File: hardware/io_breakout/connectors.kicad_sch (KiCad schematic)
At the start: 9 parts, among them J1 IDC26, J2 12-way 5.08, J3 12-way 5.08

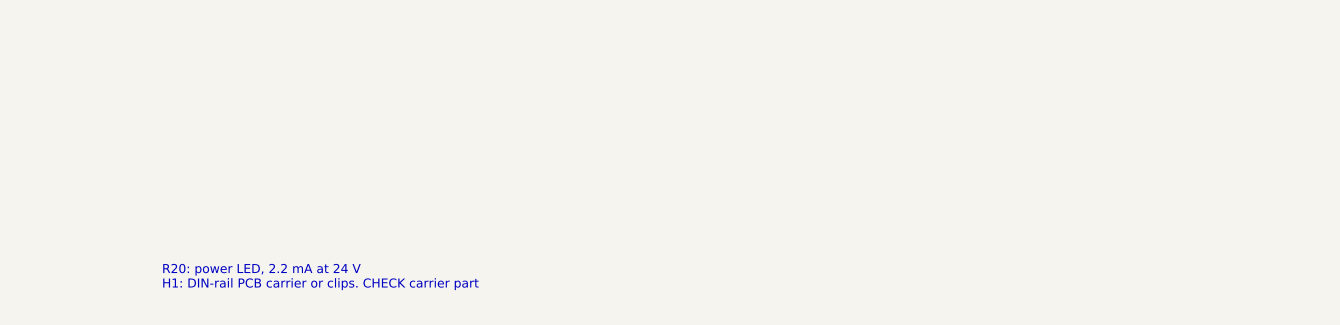
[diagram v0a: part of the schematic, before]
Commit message: CORE PCB: layout start in BC 215,6 outline; breakout header and carrier chosen
gen_pcb.py writes cems_core.kicad_pcb from design.py: 4 layers, assumed BC 215,6
outline (211.5 x 85.1 mm; BC 161,6 is too small for the I/O section), all 423
footprints with nets, connectors on the housing faces, a block plan per sheet, net
classes and 2.5 mm isolation rules between the four ground domains. Placeholder
PG-VQFN-70 footprint for the ISO2H823V2.5 (to redraw). Breakout: Wurth 61202622821
latched header, board 50 x 80 mm for a standard DIN PCB holder.

Co-Authored-By: Claude Opus 5.5 <noreply@anthropic.com>
Claude-Session: https://claude.ai/code/session_014onnq3eRiDkqdAB6fKiRDW
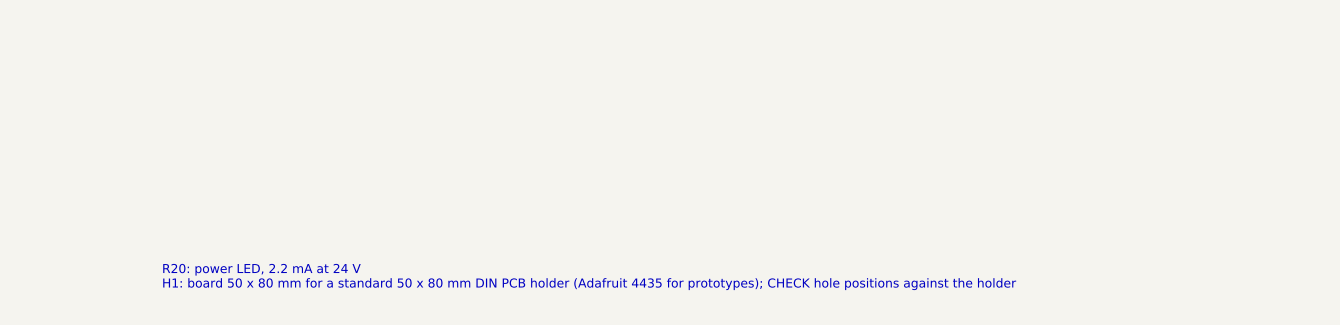
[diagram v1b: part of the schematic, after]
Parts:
- J1: MPN 26-way 2.54 mm shrouded box header with ejector latches (Wu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 -> Wurth 61202622821 (WR-BHD, 26-way, long latches, 3 A per co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
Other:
- note added: "R20: power LED, 2.2 mA at 24 V H1: board 50 x 80 mm for a standard 50 x 80 mm DIN PCB holder (Adafruit 4435 for prototypes); CHECK hole positions against the holder"
- note removed: "R20: power LED, 2.2 mA at 24 V H1: DIN-rail PCB carrier or clips. CHECK carrier part"
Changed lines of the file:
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@@
     (effects (font (size 1.0 1.0)) (justify left top))
   )
-  (text "\nR20: power LED, 2.2 mA at 24 V\nH1: DIN-rail PCB carrier or clips. CHECK carrier part"
+  (text "\nR20: power LED, 2.2 mA at 24 V\nH1: board 50 x 80 mm for a standard 50 x 80 mm DIN PCB holder (Adafruit 4435 for prototypes); CHECK hole positions against the holder"
     (at 147.32 137.16 0)
     (effects (font (size 1.0 1.0)) (justify left top))
@@
       (effects (font (size 1.27 1.27)) hide)
     )
-    (property "MPN" "26-way 2.54 mm shrouded box header with ejector latches (Wurth, Amphenol or TE), 1 A per contact. CHECK MPN" (id 4) (at 33.02 35.56 0)
+    (property "MPN" "Wurth 61202622821 (WR-BHD, 26-way, long latches, 3 A per contact; RS 771-8446)" (id 4) (at 33.02 35.56 0)
       (effects (font (size 1.27 1.27)) hide)
     )

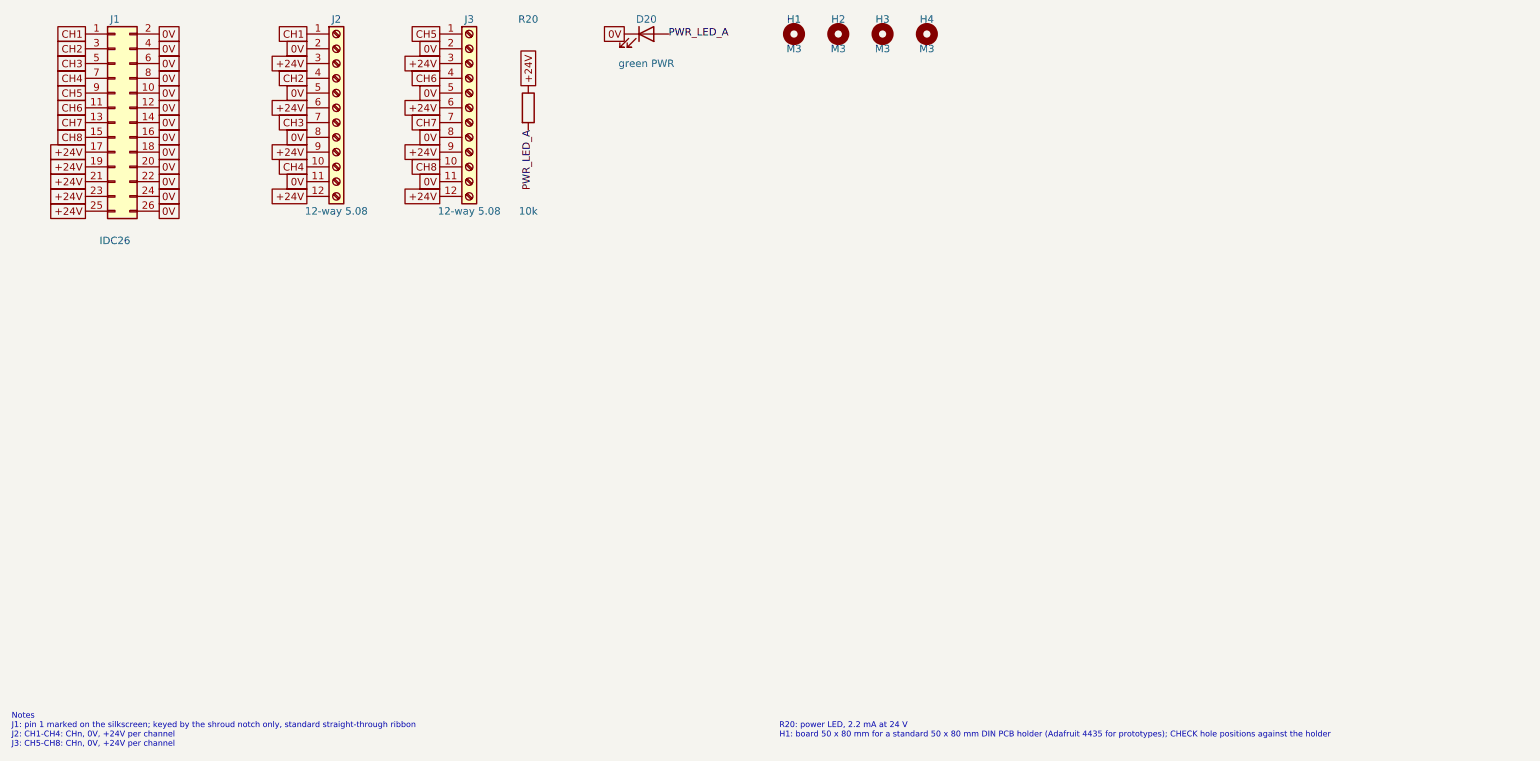
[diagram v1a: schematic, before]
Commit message: One 40-way ribbon for all digital I/O (Gary, 31 Oct)
Main board: J10 becomes a 40-way latched IDC header carrying bank A outputs 1-8 (pins
1-16, each beside its 0 V) and inputs 1-8 (pins 17-32), with 4 x +24 V and 4 x 0 V; J12
and F11 removed, so no ribbon can go into the wrong slot. Breakout rev 0.2: one board,
50 x 80 mm, two-tier 3.81 mm pluggable headers (valves OUT over 0V, inputs IN over +24V,
plus a 0V strip for 3-wire sensors), LEDs on every channel, flyback options on the valves.
Two-tier footprint is a placeholder until the maker's drawing is checked.

Co-Authored-By: Claude Opus 5.5 <noreply@anthropic.com>
Claude-Session: https://claude.ai/code/session_014onnq3eRiDkqdAB6fKiRDW
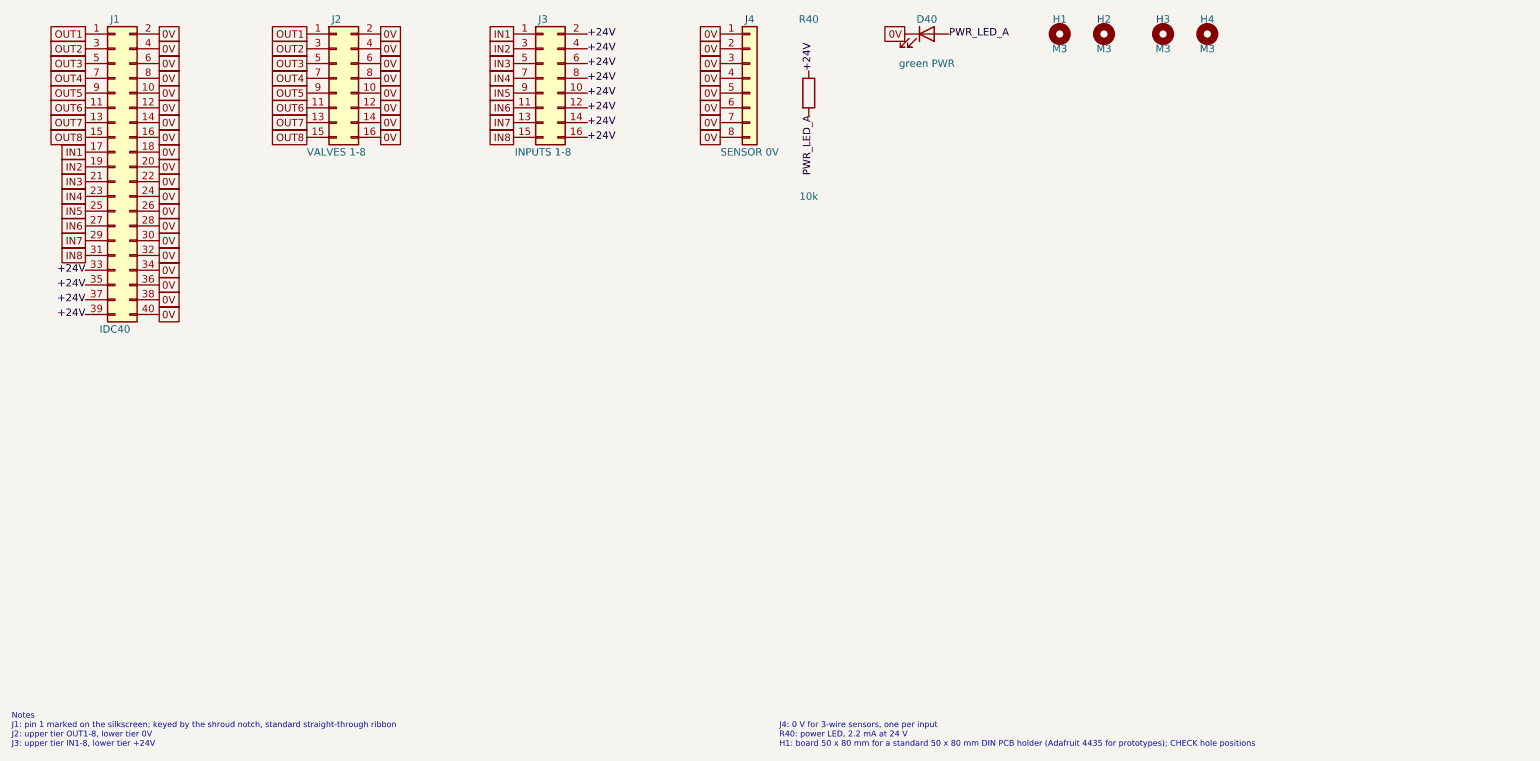
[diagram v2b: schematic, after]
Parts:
- removed D20: green PWR, LED_SMD:LED_0805_2012Metric, symbol Device:LED
- removed R20: 10k, Resistor_SMD:R_0805_2012Metric, symbol Device:R
- added D40: green PWR, LED_SMD:LED_0805_2012Metric, symbol Device:LED
- added J4: SENSOR 0V, Connector_Phoenix_MC:PhoenixContact_MCV_1,5_8-G-3.81_1x08_P3.81mm_Vertical, symbol Connector_Generic:Conn_01x08
- added R40: 10k, Resistor_SMD:R_0805_2012Metric, symbol Device:R
- J1: value IDC26 -> IDC40; footprint Connector_IDC:IDC-Header_2x13_P2.54mm_Latch_Vertical -> Connector_IDC:IDC-Header_2x20_P2.54mm_Latch_Vertical; symbol Connector_Generic:Conn_02x13_Odd_Even -> Connector_Generic:Conn_02x20_Odd_Even; MPN Wurth 61202622821 (WR-BHD, 26-way, long latches, 3 A per co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 -> Wurth 61204022821 (WR-BHD 40-way, long latches, 3 A per con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
- J2: value 12-way 5.08 -> VALVES 1-8; footprint TerminalBlock_Phoenix:TerminalBlock_Phoenix_MKDS-1,5-12-5.08_1x12_P5.08mm_Horizontal -> cems_io_breakout:Phoenix_MCDV_1,5_8-G-3.81_2x08_P3.81mm_TwoLevel; symbol Connector:Screw_Terminal_01x12 -> Connector_Generic:Conn_02x08_Odd_Even; MPN Degson or Dinkle 5.08 mm PCB screw terminal, 12-way, UL, 30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 -> Phoenix MCDV 1,5/8-G-3,81 two-level header + 2 x MCVR plugs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
- J3: value 12-way 5.08 -> INPUTS 1-8; footprint TerminalBlock_Phoenix:TerminalBlock_Phoenix_MKDS-1,5-12-5.08_1x12_P5.08mm_Horizontal -> cems_io_breakout:Phoenix_MCDV_1,5_8-G-3.81_2x08_P3.81mm_TwoLevel; symbol Connector:Screw_Terminal_01x12 -> Connector_Generic:Conn_02x08_Odd_Even; MPN Degson or Dinkle 5.08 mm PCB screw terminal, 12-way, UL, 30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 -> as J2
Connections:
- net +24V: now also J1.33 (Pin_33), J1.35 (Pin_35), J1.37 (Pin_37), J1.39 (Pin_39), J3.10 (Pin_10), J3.14 (Pin_14), J3.16 (Pin_16), J3.2 (Pin_2), J3.4 (Pin_4), J3.8 (Pin_8), R40.1; no longer J1.17 (Pin_17), J1.19 (Pin_19), J1.21 (Pin_21), J1.23 (Pin_23), J1.25 (Pin_25), J2.12 (Pin_12), J2.3 (Pin_3), J2.6 (Pin_6), J2.9 (Pin_9), J3.3 (Pin_3), J3.9 (Pin_9)
- net 0V: now also J1.28 (Pin_28), J1.30 (Pin_30), J1.32 (Pin_32), J1.34 (Pin_34), J1.36 (Pin_36), J1.38 (Pin_38), J1.40 (Pin_40), J2.10 (Pin_10), J2.12 (Pin_12), J2.14 (Pin_14), J2.16 (Pin_16), J2.4 (Pin_4), J2.6 (Pin_6), D40.1 (K), J4.1 (Pin_1), J4.2 (Pin_2), J4.3 (Pin_3), J4.4 (Pin_4), J4.5 (Pin_5), J4.6 (Pin_6), J4.7 (Pin_7), J4.8 (Pin_8); no longer J2.11 (Pin_11), J2.5 (Pin_5), J3.11 (Pin_11), J3.2 (Pin_2), J3.5 (Pin_5), J3.8 (Pin_8)
- net PWR_LED_A: now also D40.2 (A), R40.2
- net CH1 renamed OUT1
- net CH2 renamed OUT2
- net OUT2: now also J2.3 (Pin_3); no longer J2.4 (Pin_4)
- net CH3 renamed OUT3
- net OUT3: now also J2.5 (Pin_5); no longer J2.7 (Pin_7)
- net CH4 renamed OUT4
- net OUT4: now also J2.7 (Pin_7); no longer J2.10 (Pin_10)
- net CH5 renamed IN1
- net IN1: now also J1.17 (Pin_17); no longer J1.9 (Pin_9)
- net CH6 renamed OUT6
- net OUT6: now also J2.11 (Pin_11); no longer J3.4 (Pin_4)
- net CH7 renamed IN4
- net IN4: now also J1.23 (Pin_23); no longer J1.13 (Pin_13)
- net CH8 renamed OUT8
- net OUT8: now also J2.15 (Pin_15); no longer J3.10 (Pin_10)
- new net IN2: J1.19 (Pin_19), J3.3 (Pin_3)
- new net IN3: J1.21 (Pin_21), J3.5 (Pin_5)
- new net IN5: J1.25 (Pin_25), J3.9 (Pin_9)
- new net IN6: J1.27 (Pin_27), J3.11 (Pin_11)
- new net IN7: J1.29 (Pin_29), J3.13 (Pin_13)
- new net IN8: J1.31 (Pin_31), J3.15 (Pin_15)
- new net OUT5: J1.9 (Pin_9), J2.9 (Pin_9)
- new net OUT7: J1.13 (Pin_13), J2.13 (Pin_13)
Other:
- note added: "J4: 0 V for 3-wire sensors, one per input R40: power LED, 2.2 mA at 24 V H1: board 50 x 80 mm for a standard 50 x 80 mm DIN PCB holder (Adafruit 4435 for prototypes); CHECK hole positions"
- note added: "Notes J1: pin 1 marked on the silkscreen; keyed by the shroud notch, standard straight-through ribbon J2: upper tier OUT1-8, lower tier 0V J3: upper tier IN1-8, lower tier +24V"
- note removed: "Notes J1: pin 1 marked on the silkscreen; keyed by the shroud notch only, standard straight-through ribbon J2: CH1-CH4: CHn, 0V, +24V per channel J3: CH5-CH8: CHn, 0V, +24V per channel"
- note removed: "R20: power LED, 2.2 mA at 24 V H1: board 50 x 80 mm for a standard 50 x 80 mm DIN PCB holder (Adafruit 4435 for prototypes); CHECK hole positions against the holder"
- moved on the sheet: H1, H2, H3, H4

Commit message: CORE PCB + breakout: make every user plug fit only its own header
Three pitch families (5.08 power/24 V outputs, 3.81 bank B, 3.5 sensors), one size per
header except the harmless temperature and 4-20 mA groups, and a coding key per header
(script-checked against every plug and shift). J13+J14 merged into one 4-way field plug;
pump power and signals on one 6-way plug (J16 gone); relays 3-way. Survival layer: 1k 1 W
pump outputs, per-channel relay PTCs + CPC1014N, 30 mA loop current limiters, TVS on the
5 V and 10 V sensor supplies. CORE_PCB.md section 15 has the mis-plug tables.

Co-Authored-By: Claude Opus 5.5 <noreply@anthropic.com>
Claude-Session: https://claude.ai/code/session_014onnq3eRiDkqdAB6fKiRDW
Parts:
- J2: MPN Phoenix MCDV 1,5/8-G-3,81 two-level header + 2 x MCVR plugs (or Degson/Dinkle equivalent). CHECK MPN and footprint -> Phoenix MCDV 1,5/8-G-3,81 two-level header + 2 x MCVR plugs (or Degson/Dinkle equivalent). Coding keys: upper tier pin 1, lower tier pin 2 (plugs coded to match). CHECK MPN, footprint, coding parts
- J3: MPN as J2 -> as J2; coding keys: upper tier pin 3, lower tier pin 4
- J4: MPN Phoenix MCV 1,5/8-G-3,81 + plug -> Phoenix MCV 1,5/8-G-3,81 + plug; coding key at pin 5
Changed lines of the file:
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@@
       (effects (font (size 1.27 1.27)) hide)
     )
-    (property "MPN" "Phoenix MCDV 1,5/8-G-3,81 two-level header + 2 x MCVR plugs (or Degson/Dinkle equivalent). CHECK MPN and footprint" (id 4) (at 71.12 27.94 0)
+    (property "MPN" "Phoenix MCDV 1,5/8-G-3,81 two-level header + 2 x MCVR plugs (or Degson/Dinkle equivalent). Coding keys: upper tier pin 1, lower tier pin 2 (plugs coded to match). CHECK MPN, footprint, coding parts" (id 4) (at 71.12 27.94 0)
       (effects (font (size 1.27 1.27)) hide)
     )
@@
       (effects (font (size 1.27 1.27)) hide)
     )
-    (property "MPN" "as J2" (id 4) (at 106.68 27.94 0)
+    (property "MPN" "as J2; coding keys: upper tier pin 3, lower tier pin 4" (id 4) (at 106.68 27.94 0)
       (effects (font (size 1.27 1.27)) hide)
     )
@@
       (effects (font (size 1.27 1.27)) hide)
     )
-    (property "MPN" "Phoenix MCV 1,5/8-G-3,81 + plug" (id 4) (at 142.24 27.94 0)
+    (property "MPN" "Phoenix MCV 1,5/8-G-3,81 + plug; coding key at pin 5" (id 4) (at 142.24 27.94 0)
       (effects (font (size 1.27 1.27)) hide)
     )
